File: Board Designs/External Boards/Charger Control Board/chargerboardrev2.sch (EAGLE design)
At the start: 20 parts, among them J1 JUMPER.1, X1 CONNECTOR-6NANO-FIT_VERTICAL-6, X3 CONNECTOR-2, X4 CONNECTOR-2

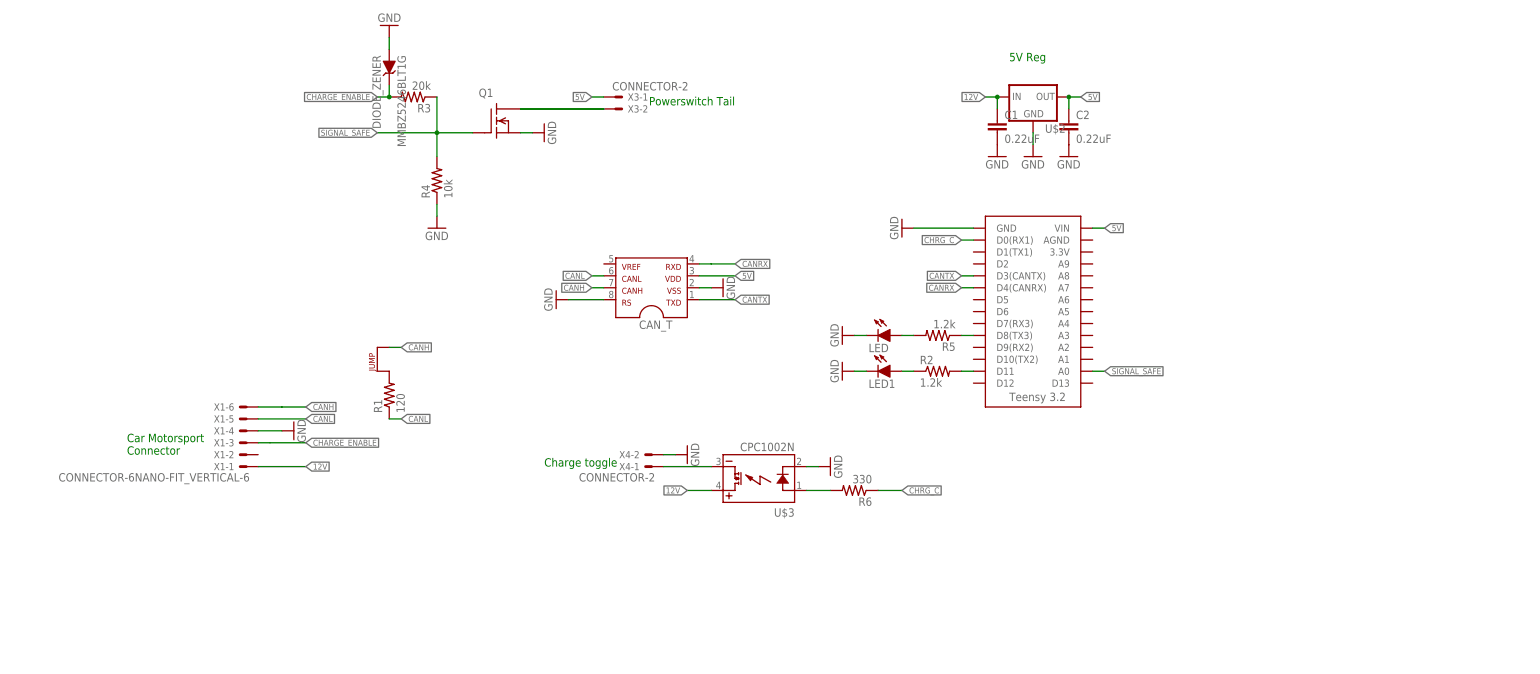
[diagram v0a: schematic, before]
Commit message: Adjusted schematic for v2 of charger control board
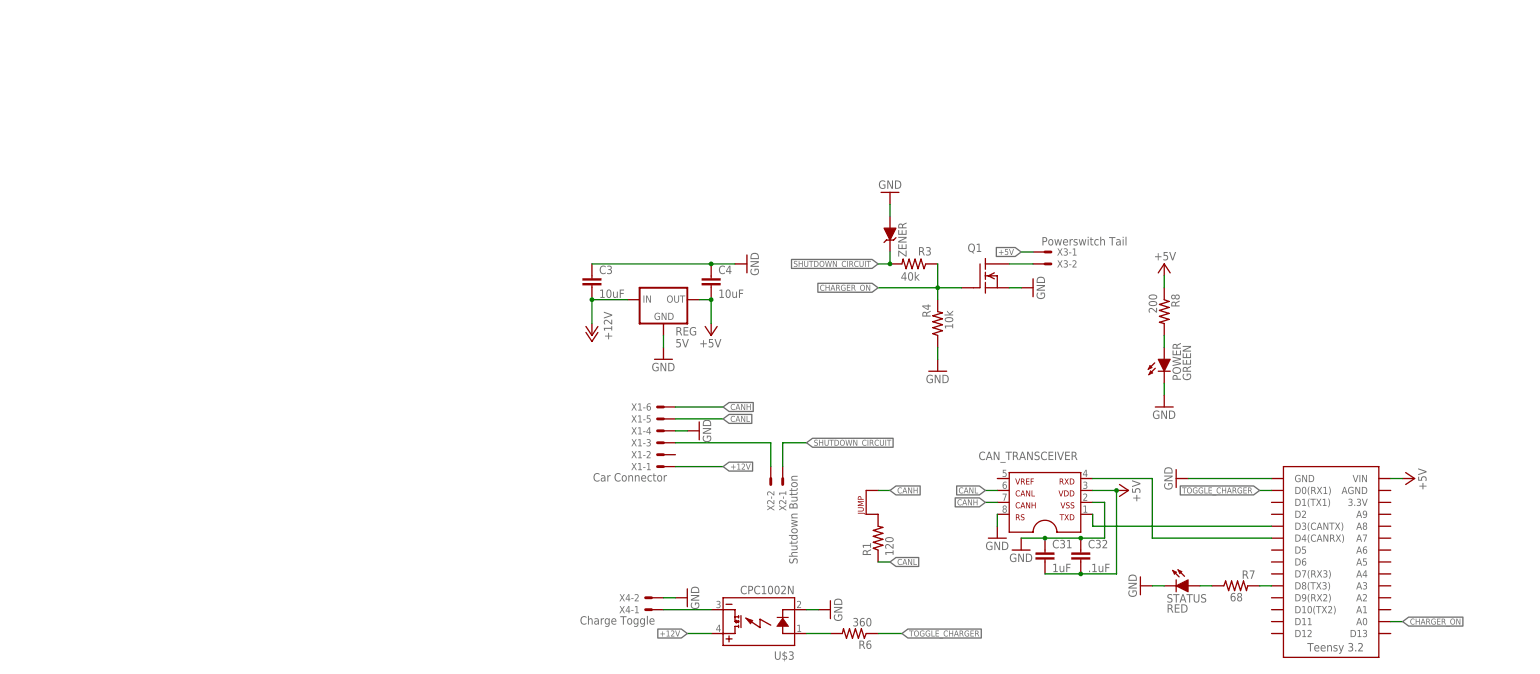
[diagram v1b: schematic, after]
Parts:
- removed C1, C2: 0.22uF, HyTechDevices:CAP0805
- removed CAN_T: MCP2551, HyTechDevices:MCP2551
- removed LED, LED1: (no value), HyTechDevices:LED-0805
- removed MMBZ5246BLT1G: DIODE_ZENER, HyTechDevices:DIODE_ZENER
- removed R2, R5: 1.2k, HyTechDevices:RESISTOR0805-RES
- removed U$1: TEENSY_3.2_SIMPLE, HyTechDevices:TEENSY_3.2_SIMPLE
- removed U$2: (no value), HyTechDevices:5VREG_LM340-NLM340MPX-5.0/NOPB
- added C3, C4: 10uF, HyTechDevices:CAP0805
- added C31: 1uF, HyTechDevices:CAP0805
- added C32: .1uF, HyTechDevices:CAP0805
- added CAN_TRANSCEIVER: MCP2551, HyTechDevices:MCP2551
- added POWER: GREEN, HyTechDevices:LED-0805
- added R7: 68, HyTechDevices:RESISTOR0805-RES
- added R8: 200, HyTechDevices:RESISTOR0805-RES
- added REG: 5V, HyTechDevices:OKI-78SR-5
- added STATUS: RED, HyTechDevices:LED-0805
- added U$4: TEENSY_3.2_SIMPLE, HyTechDevices:TEENSY_3.2_SIMPLE
- added X2: Shutdown Button, HyTechDevices:CONNECTOR-2
- added ZENER: DIODE_ZENER, HyTechDevices:DIODE_ZENER
- R3: value 20k -> 40k
- R6: value 330 -> 360
- X1: value CONNECTOR-6NANO-FIT_VERTICAL-6 -> Car Connector
- X3: value CONNECTOR-2 -> Powerswitch Tail
- X4: value CONNECTOR-2 -> Charge Toggle
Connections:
- removed net 12V: C1.1, U$2.IN, U$3.DC+, X1-1.S
- removed net 5V: C2.1, CAN_T.3, U$1.VIN, U$2.OUT, X3-1.S
- removed net CANRX: CAN_T.4, U$1.D4(CANRX)
- removed net CANTX: CAN_T.1, U$1.D3(CANTX)
- removed net CHARGE_ENABLE: MMBZ5246BLT1G.C, R3.2, X1-3.S
- removed net CHRG_C: R6.1, U$1.D0(RX1)
- removed net N$2: R2.2, U$1.D11
- removed net N$3: R5.1, U$1.D8(TX3)
- removed net N$4: LED1.A, R2.1
- removed net N$6: LED.A, R5.2
- removed net SIGNAL_SAFE: Q1.G, R3.1, R4.2, U$1.A0
- new net +12V: C3.2, REG.IN, U$3.DC+, X1-1.S
- new net +5V: C31.2, C32.2, C4.2, CAN_TRANSCEIVER.3, R8.1, REG.OUT, U$4.VIN, X3-1.S
- new net CHARGER_ON: Q1.G, R3.1, R4.2, U$4.A0
- new net N$11: R7.2, U$4.D8(TX3)
- new net N$15: CAN_TRANSCEIVER.4, U$4.D4(CANRX)
- new net N$22: CAN_TRANSCEIVER.1, U$4.D3(CANTX)
- new net N$8: R7.1, STATUS.A
- new net N$9: POWER.A, R8.2
- new net SHUTDOWN_CIRCUIT: R3.2, X1-3.S, X2-1.S, X2-2.S, ZENER.C
- new net TOGGLE_CHARGER: R6.1, U$4.D0(RX1)
- net CANH: now also CAN_TRANSCEIVER.7; no longer CAN_T.7
- net CANL: now also CAN_TRANSCEIVER.6; no longer CAN_T.6
- net GND: now also C3.1, C31.1, C32.1, C4.1, CAN_TRANSCEIVER.2, CAN_TRANSCEIVER.8, POWER.C, REG.GND, STATUS.C, U$4.GND, ZENER.A; no longer C1.2, C2.2, CAN_T.2, CAN_T.8, LED.C, LED1.C, MMBZ5246BLT1G.A, U$1.GND, U$2.GND
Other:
- note removed: "5V Reg"
- note removed: "Car Motorsport Connector"
- note removed: "Charge toggle"
- note removed: "Powerswitch Tail"
- moved on the sheet: Q1, R1, R3, R4, R6, U$3, X1-1, X1-2, X1-3, X1-4, X1-5, X1-6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

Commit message: Finished charger control board rev 2
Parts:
- removed J1: JUMPER.1, HyTechDevices:JUMPER.1
- added C5: 4.7nF, HyTechDevices:CAP0805
- added CAN_TERM_JMP: M02_SLIM, HyTechDevices:M02_SLIM
- added R2: 60, HyTechDevices:RESISTOR0805-RES
- added U$13: CDSOT23-T24CAN-Q, HyTechDevices:CDSOT23-T24CAN-Q
- added ZENER1: DIODE, HyTechDevices:DIODE0805
- R1: value 120 -> 60
- renumbered C31 to C1, C32 to C2, R8 to R5
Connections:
- removed net N$5: J1.P$1, R1.2
- new net N$17: CAN_TERM_JMP.2, R2.2
- new net N$62: C5.1, R1.2, R2.1
- new net PRE_BRB_SHUTDOWN_CIRCUIT: X1-3.S, X2-2.S
- new net PRE_DIODE_CHARGER_ON: U$4.A0, ZENER1.C
- net CANH: now also CAN_TERM_JMP.1, U$13.2; no longer J1.P$2
- net CANL: now also U$13.1
- net CHARGER_ON: now also ZENER1.A; no longer U$4.A0
- net GND: now also C5.2, U$13.3
- net SHUTDOWN_CIRCUIT: no longer X1-3.S, X2-2.S
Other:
- moved on the sheet: R1

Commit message: Fixed small board issues and exported gerbers
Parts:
- renumbered ZENER1 to DIODE
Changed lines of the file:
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@@
 <part name="GND16" library="HyTechSymbols" deviceset="GND" device=""/>
 <part name="X2" library="HyTechDevices" deviceset="CONNECTOR-2" device="" value="Shutdown Button"/>
-<part name="ZENER1" library="HyTechDevices" deviceset="DIODE" device="0805" value="DIODE"/>
+<part name="DIODE" library="HyTechDevices" deviceset="DIODE" device="0805" value="DIODE"/>
 <part name="R1" library="HyTechDevices" deviceset="RESISTOR" device="0805-RES" value="60"/>
 <part name="CAN_TERM_JMP" library="HyTechDevices" deviceset="M02" device="_SLIM" value="M02_SLIM"/>
@@
 <attribute name="VALUE" x="-39.243" y="5.842" size="1.778" layer="96" rot="R270"/>
 </instance>
-<instance part="ZENER1" gate="1" x="-15.24" y="45.72" smashed="yes" rot="R180">
+<instance part="DIODE" gate="1" x="-15.24" y="45.72" smashed="yes" rot="R180">
 <attribute name="VALUE" x="-11.43" y="44.2214" size="1.778" layer="96" rot="R180"/>
 </instance>
@@
 <segment>
 <wire x1="-17.78" y1="45.72" x2="-20.32" y2="45.72" width="0.1524" layer="91"/>
-<pinref part="ZENER1" gate="1" pin="C"/>
+<pinref part="DIODE" gate="1" pin="C"/>
 <label x="-20.32" y="45.72" size="1.27" layer="95" rot="R180" xref="yes"/>
 </segment>
@@
 <pinref part="Q1" gate="G$1" pin="G"/>
 <wire x1="-7.62" y1="45.72" x2="-10.16" y2="45.72" width="0.1524" layer="91"/>
-<pinref part="ZENER1" gate="1" pin="A"/>
-</segment>
-</net>
+<pinref part="DIODE" gate="1" pin="A"/>
+</segment>
+</net>
